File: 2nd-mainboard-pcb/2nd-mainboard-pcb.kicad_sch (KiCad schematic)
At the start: 29 parts, among them J1 PJ-082BH, U1 SQJ409EP-T1_GE3, U2 SZ1SMB5927BT3G, U3 TPS56837HRPAR, U4 TPS565208

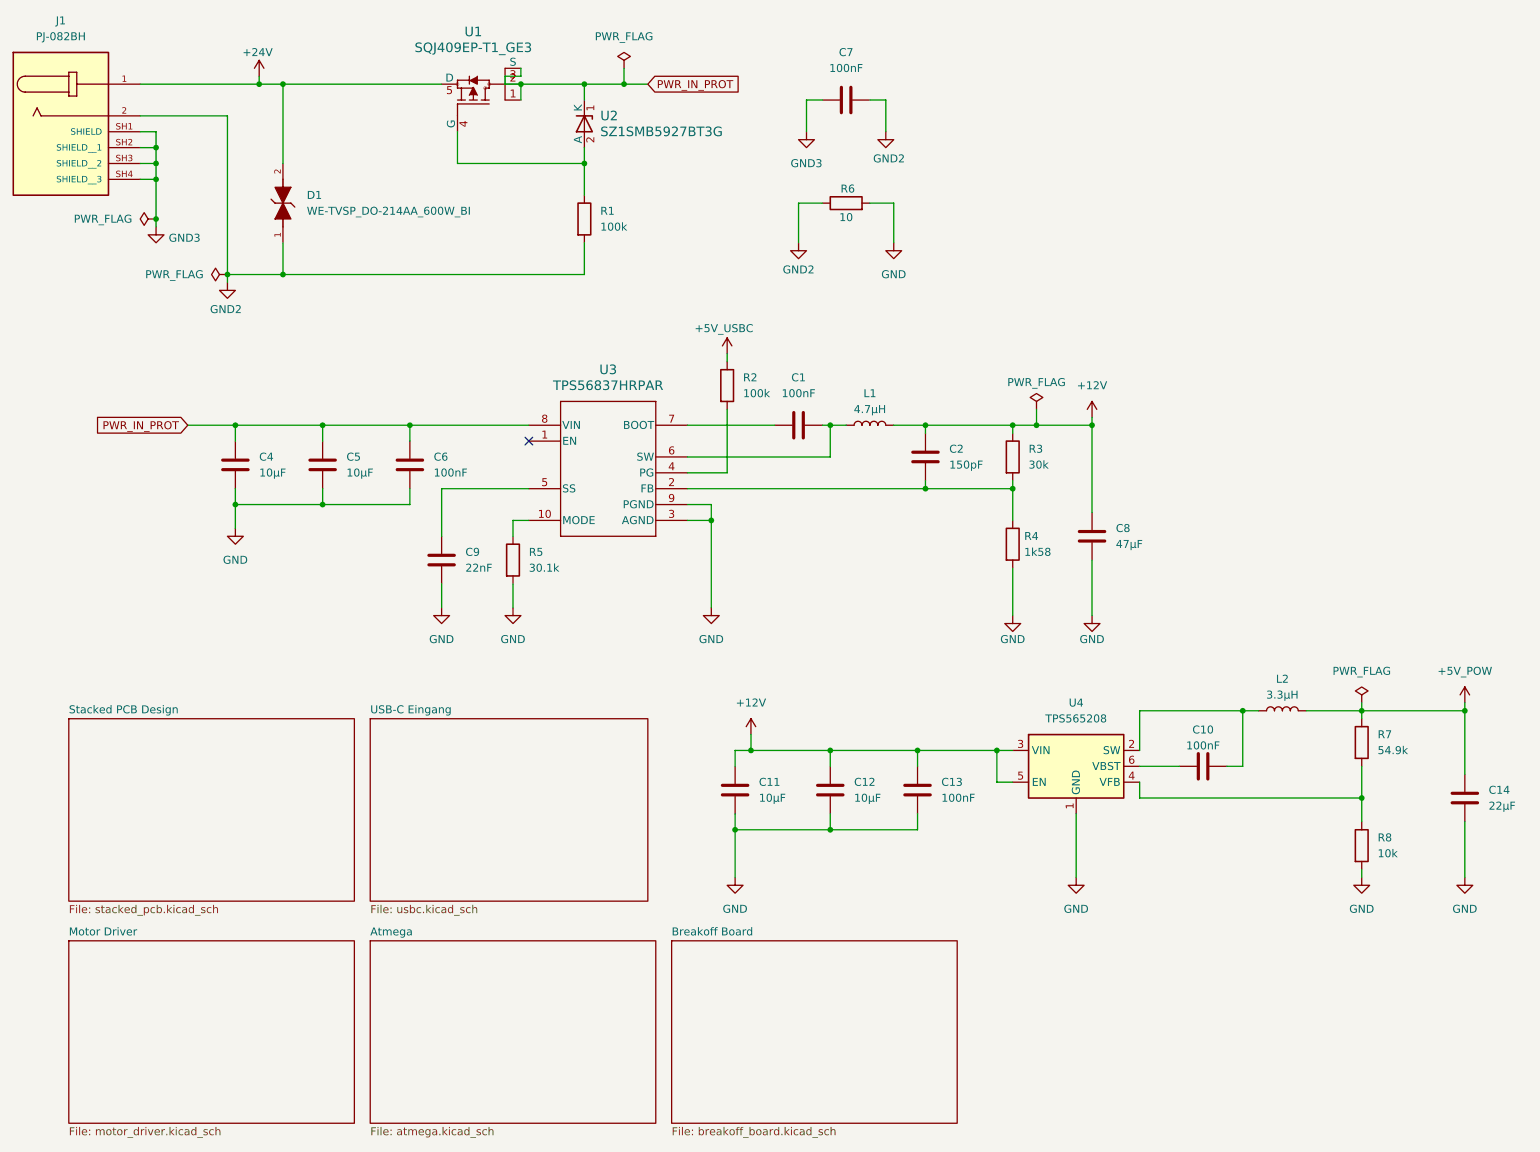
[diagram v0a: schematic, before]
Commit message: volle zonen auf b.cu erstellt und schaltregler symbol ausgetauscht
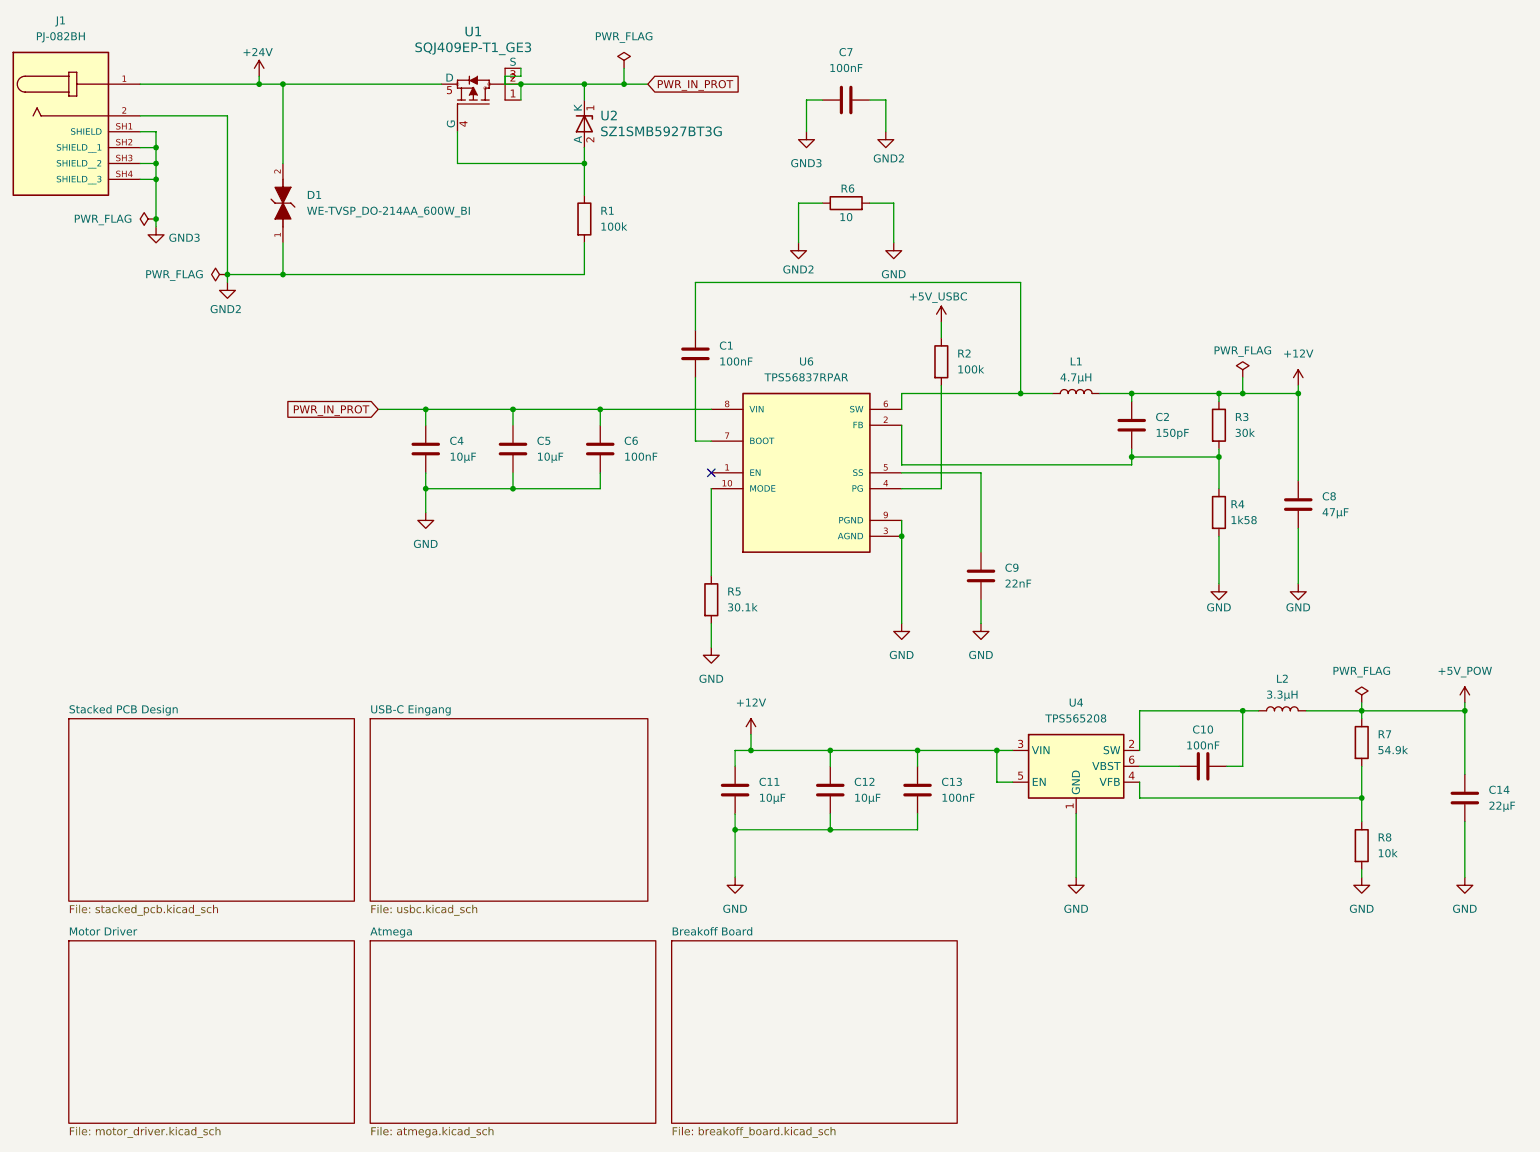
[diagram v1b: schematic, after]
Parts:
- removed U3: TPS56837HRPAR, Imported_Component_Footprints:TPS56837HRPAR, symbol Imported_Component_Symbols:TPS56837HRPAR
- added U6: TPS56837RPAR, Imported_Component_Footprints:CONV_TPS56837RPAR, symbol Imported_Component_Symbols:TPS56837RPAR
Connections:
- net GND: now also U6.3 (AGND), U6.9 (PGND)
- net PWR_IN_PROT: now also U6.8 (VIN)
- net at R5.1: now also U6.10 (MODE)
- net at C2.2, R3.2, R4.1: now also U6.2 (FB)
- net at R2.2: now also U6.4 (PG)
- net at C9.1: now also U6.5 (SS)
- net at C1.2, L1.1: now also U6.6 (SW)
- net at C1.1: now also U6.7 (BOOT)
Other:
- moved on the sheet: C1, C2, C4, C5, C6, C8, C9, L1, R2, R3, R4, R5

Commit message: last few changes
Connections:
- net +24V: now also U1.1, U1.2, U1.3 (S); no longer U1.5 (D)
- net PWR_IN_PROT: now also U1.5 (D); no longer U1.1, U1.2, U1.3 (S)
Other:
- moved on the sheet: D1, L2, U1
